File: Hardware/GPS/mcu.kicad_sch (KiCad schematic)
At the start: 1 part, among them U1 STM32H735ZGTx

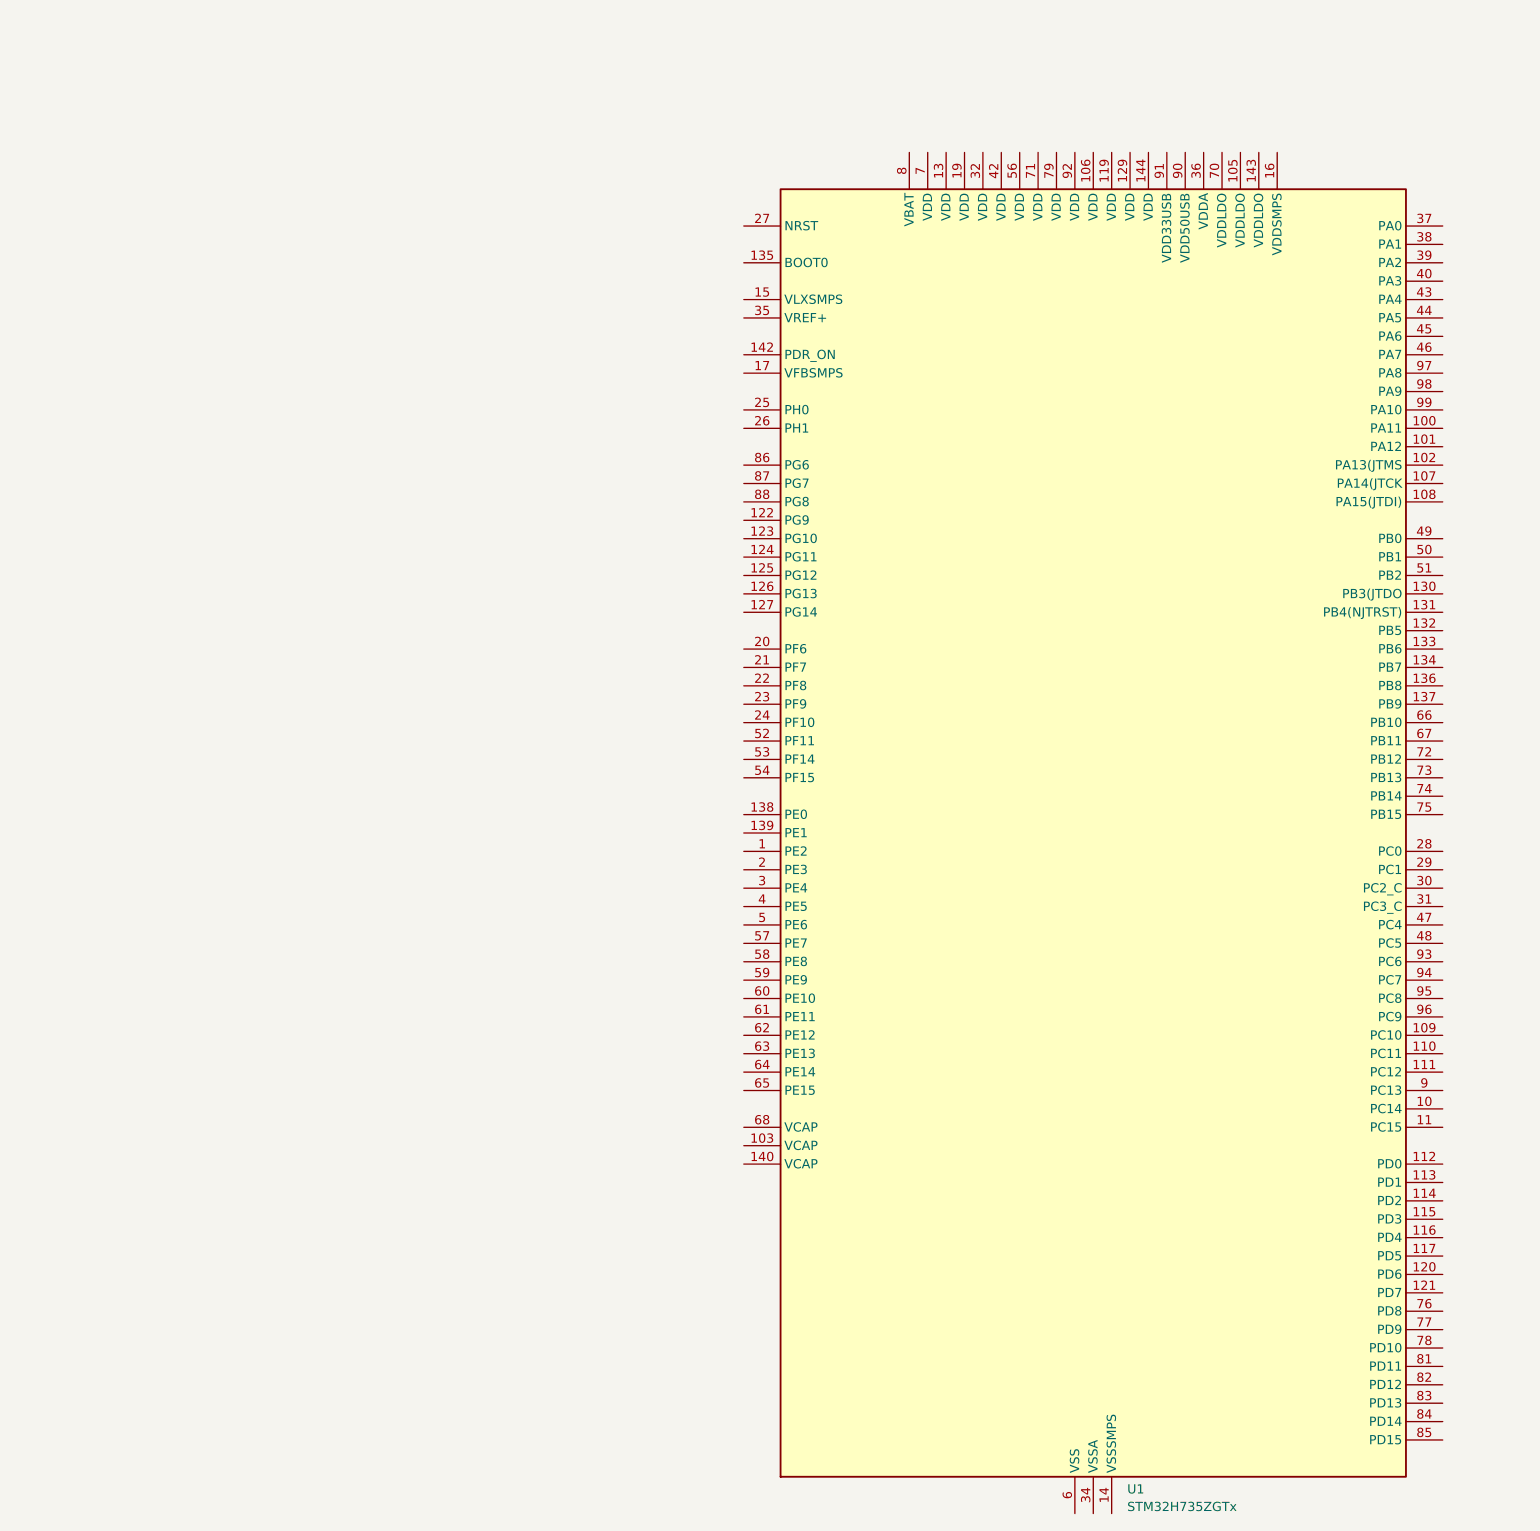
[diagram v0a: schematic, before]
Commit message: Major updates to Simulator and hardware
- Simulator has functional acquisition for L1CA, E1C, B1C, L1C.
- Simulator can track, decode, and solve for position on L1CA and E1C.
- Development on custom hardware
- Created Pi Pico 2 development environment for prototyping.
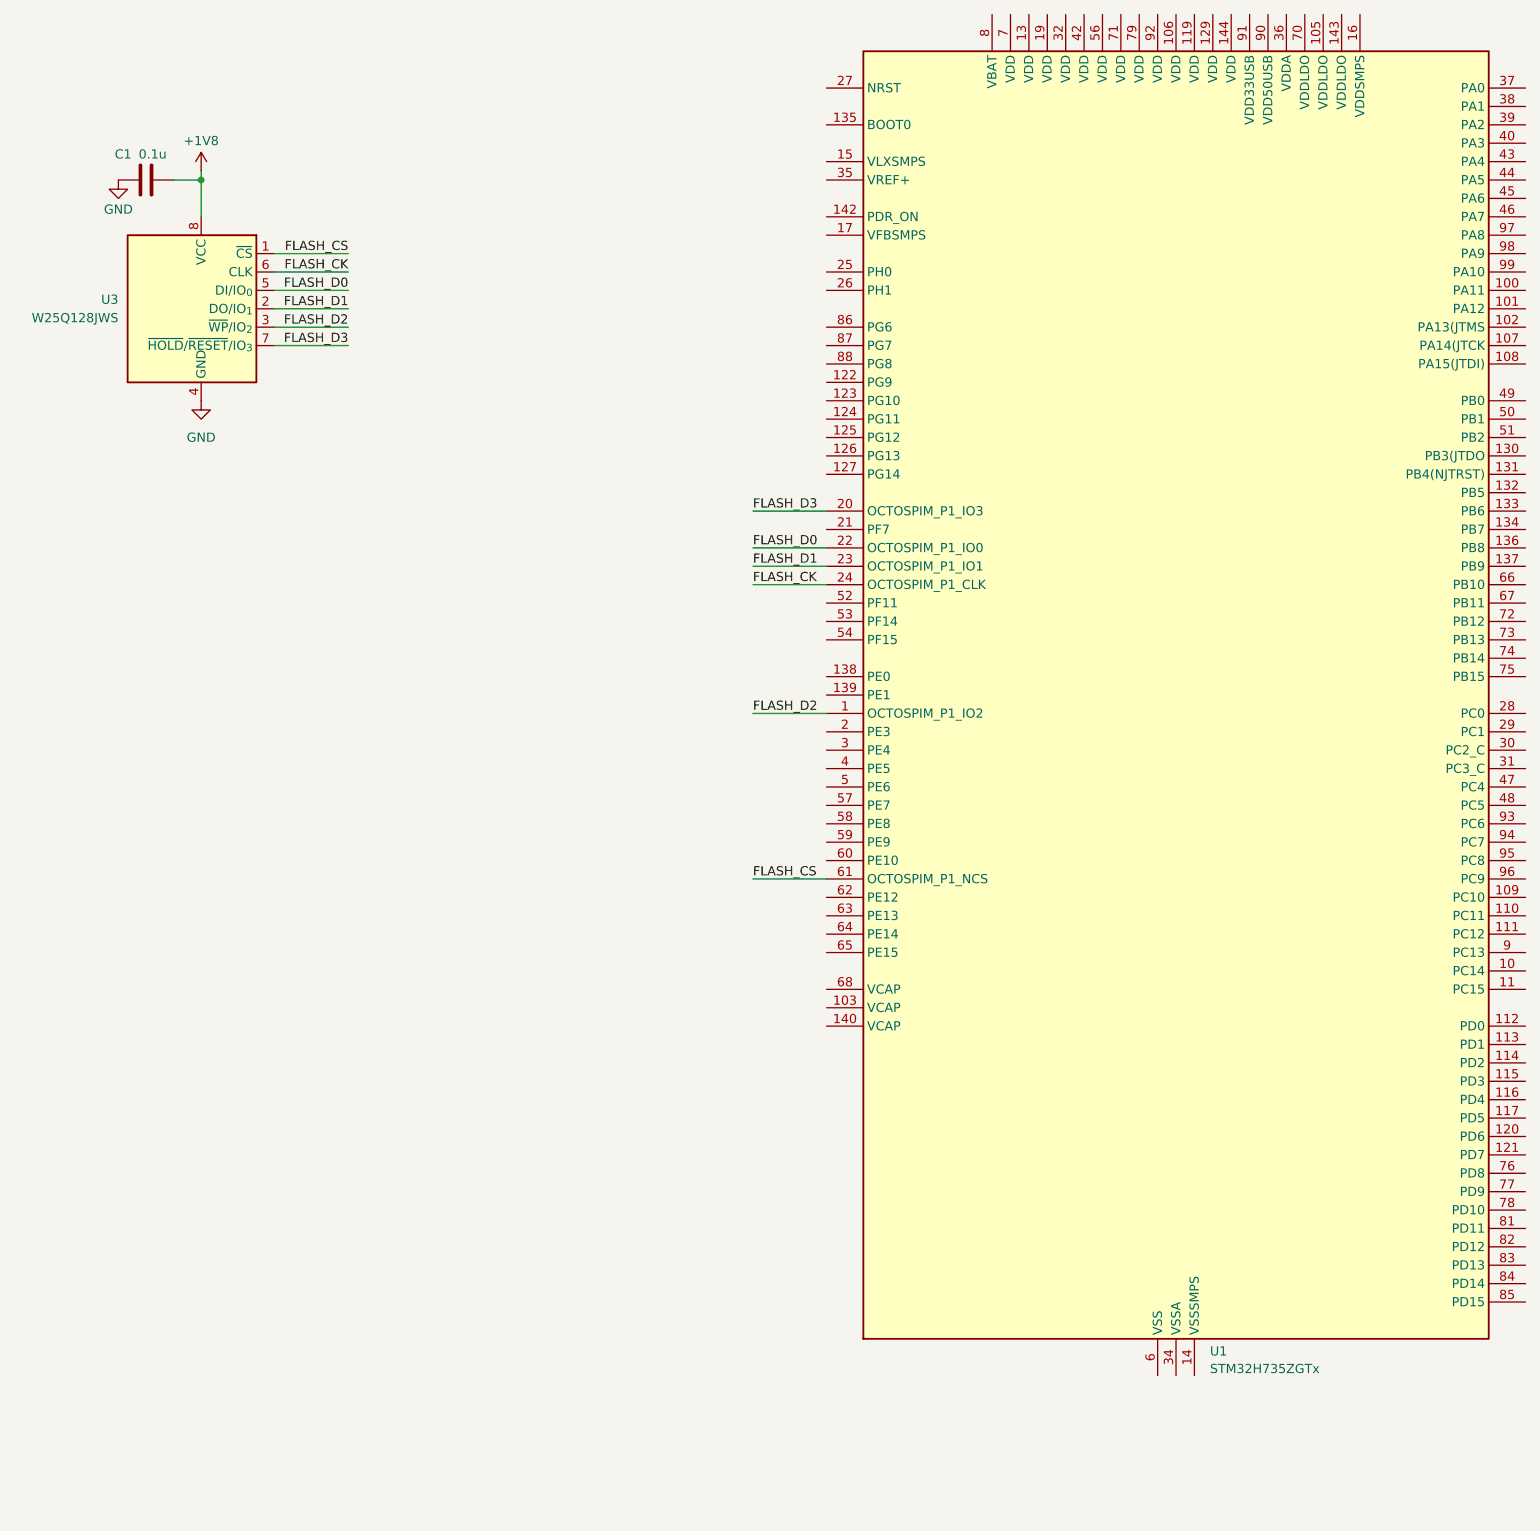
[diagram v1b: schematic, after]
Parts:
- added C1: 0.1u, symbol Device:C
- added U3: W25Q128JWS, Package_SO:SOIC-8_5.3x5.3mm_P1.27mm, symbol Memory_Flash:W25Q128JVS
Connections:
- net FLASH_D2: now reaches U1.1 (PE2)
- net FLASH_D2: now also U3.3 (~{WP}/IO_{2})
- net FLASH_D3: now reaches U1.20 (PF6)
- net FLASH_D3: now also U3.7 (~{HOLD}/~{RESET}/IO_{3})
- net FLASH_D0: now reaches U1.22 (PF8)
- net FLASH_D0: now also U3.5 (DI/IO_{0})
- net FLASH_D1: now reaches U1.23 (PF9)
- net FLASH_D1: now also U3.2 (DO/IO_{1})
- net FLASH_CK: now reaches U1.24 (PF10)
- net FLASH_CK: now also U3.6 (CLK)
- net FLASH_CS: now reaches U1.61 (PE11)
- net FLASH_CS: now also U3.1 (~{CS})
- new net +1V8: C1.1, U3.8 (VCC)
- new net GND: C1.2, U3.4 (GND)
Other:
- moved on the sheet: U1
